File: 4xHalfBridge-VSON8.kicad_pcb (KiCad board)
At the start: 4 copper layers, 90 x 36 mm, 87 parts, among them U1 VSON8_Nexfet, U10 24LC01, U2 VSON8_Nexfet, U3 VSON8_Nexfet, U4 VSON8_Nexfet, U5 VSON8_Nexfet, U6 VSON8_Nexfet, U7 VSON8_Nexfet, U8 VSON8_Nexfet, U9 PowerStage_L

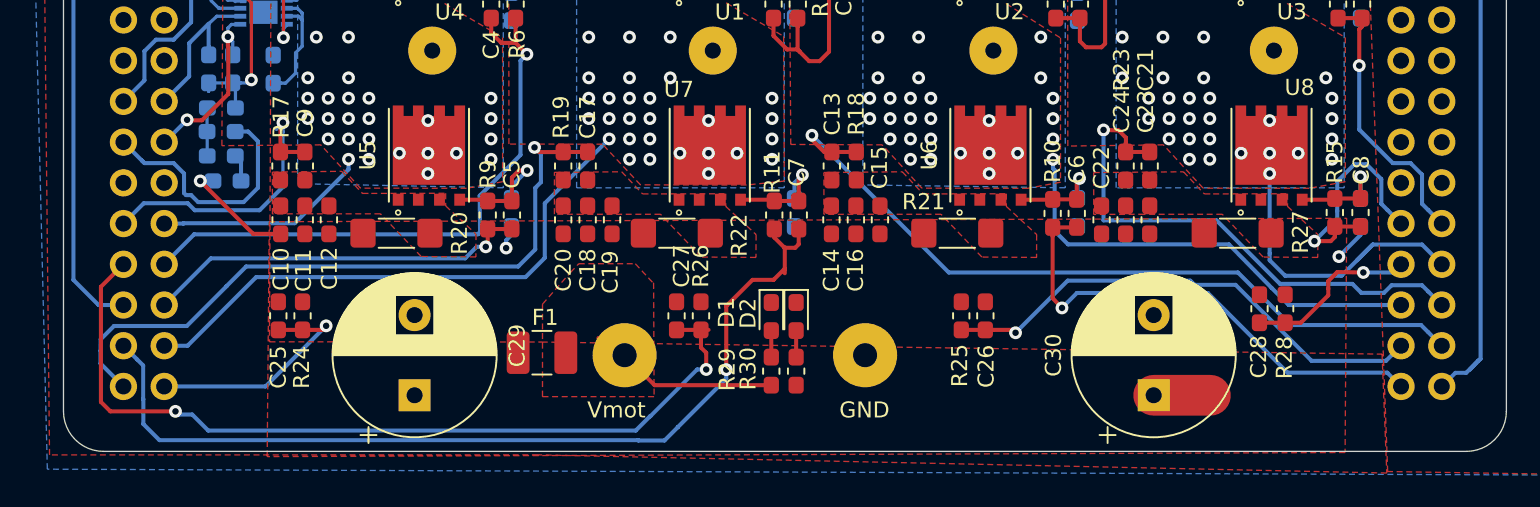
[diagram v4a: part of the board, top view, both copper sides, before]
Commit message: add voltage divider circuit for motor coil outpus
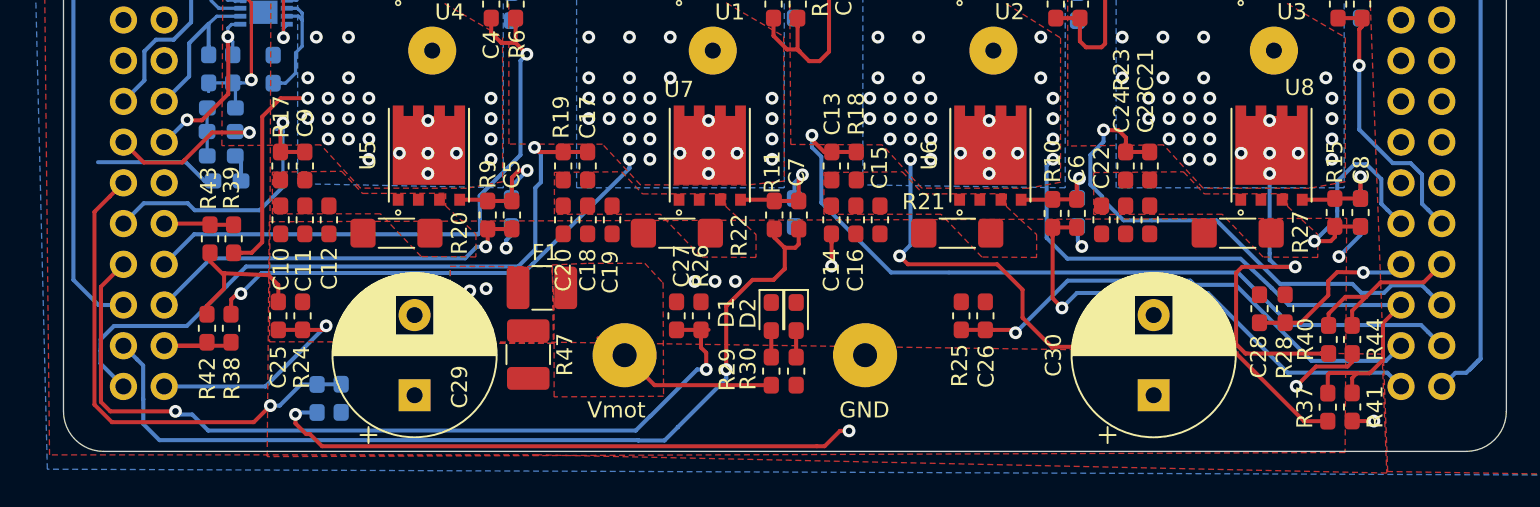
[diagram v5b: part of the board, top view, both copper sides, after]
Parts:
- added R37: R, Resistor_SMD:R_0603_1608Metric_Pad1.05x0.95mm_HandSolder, F.Cu at (78.9, 33.2)
- added R38: R, Resistor_SMD:R_0603_1608Metric_Pad1.05x0.95mm_HandSolder, F.Cu at (10.4, 28.3)
- added R39: R, Resistor_SMD:R_0603_1608Metric_Pad1.05x0.95mm_HandSolder, F.Cu at (10.6, 22.7)
- added R40: R, Resistor_SMD:R_0603_1608Metric_Pad1.05x0.95mm_HandSolder, F.Cu at (78.9, 29.0)
- added R41: R, Resistor_SMD:R_0603_1608Metric_Pad1.05x0.95mm_HandSolder, F.Cu at (80.4, 33.2)
- added R42: R, Resistor_SMD:R_0603_1608Metric_Pad1.05x0.95mm_HandSolder, F.Cu at (8.95, 28.3)
- added R43: R, Resistor_SMD:R_0603_1608Metric_Pad1.05x0.95mm_HandSolder, F.Cu at (9.14, 22.7)
- added R44: R, Resistor_SMD:R_0603_1608Metric_Pad1.05x0.95mm_HandSolder, F.Cu at (80.4, 29.0)
- added R45: R, Resistor_SMD:R_0603_1608Metric_Pad1.05x0.95mm_HandSolder, B.Cu at (15.8, 32.7)
- added R46: R, Resistor_SMD:R_0603_1608Metric_Pad1.05x0.95mm_HandSolder, B.Cu at (17.3, 32.7)
- added R47: R, Resistor_SMD:R_1210_3225Metric_Pad1.42x2.65mm_HandSolder, F.Cu at (29.0, 30.0)
- moved F1 4.05 mm to (29.8, 25.8)
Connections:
- C29 pad 1: /VDRAIN -> /MISENN
- C30 pad 1: /VDRAIN -> /MISENN
- C31 pad 1: /VDRAIN -> /MISENN
- C32 pad 1: /VDRAIN -> /MISENN
- C33 pad 1: /VDRAIN -> /MISENN
- C34 pad 1: /VDRAIN -> /MISENN
- F1 pad 1: /VDRAIN -> /MISENP
- R30 pad 2: /VDRAIN -> /MISENN
- U1 pad 3: /VDRAIN -> /MISENN
- U2 pad 3: /VDRAIN -> /MISENN
- U3 pad 3: /VDRAIN -> /MISENN
- U4 pad 3: /VDRAIN -> /MISENN
- U9 pad 13: Net-(U9-Pad13) -> /VSEN_VMOT
- U9 pad 16: /A -> /VSENA
- U9 pad 22: /B -> /VSENB
- U9 pad 42: /D -> /VSEND
- U9 pad 43: /C -> /VSENC
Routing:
- net /VSENC: track 0.00 -> 39.1 mm, vias 0 -> 1
- net /MISENN: track 0.00 -> 37.5 mm, vias 0 -> 22
- net /VSEN_VMOT: track 0.00 -> 31.4 mm, vias 0 -> 1
- net GND: track 21.0 -> 40.6 mm, vias 5 -> 11
- net /VSEND: track 0.00 -> 11.2 mm
- net /C: track 28.0 -> 38.3 mm
- net /VSENB: track 0.00 -> 7.02 mm
- net /5V: track 15.7 -> 10.2 mm, vias 0 -> 1
- net /B: track 40.3 -> 34.9 mm
- net /VSENA: track 0.00 -> 4.36 mm
- net /VDRAIN: track 3.54 -> 0.00 mm, vias 20 -> 0
- net /D: track 19.2 -> 21.5 mm, vias 29 -> 30
- net /CISENP: track 48.1 -> 50.2 mm
- net /A: track 13.5 -> 13.2 mm, vias 26 -> 25
- net /MISENP: vias 0 -> 5
- added copper zone on F.Cu, net /MISENN
- added copper zone on B.Cu, net /MISENP
- added copper zone on F.Cu, net /MISENP
- removed copper zone on F.Cu, net /VDRAIN
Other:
- copper layers 4 -> 2

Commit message: add files
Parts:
- removed C20, C21, C22, C23, C24, C25, C26, C27, C28: C, Capacitor_SMD:C_0603_1608Metric_Pad1.05x0.95mm_HandSolder
- removed C29, C30: CP, Capacitor_THT:CP_Radial_D10.0mm_P5.00mm
- removed C31, C32, C33, C34: CP, Capacitor_THT:CP_Radial_D5.0mm_P2.50mm
- removed C35: X7R, 47-nF, Capacitor_SMD:C_0603_1608Metric_Pad1.05x0.95mm_HandSolder
- removed the D2 at (45.7, 27.6)
- removed R40, R41, R42, R43, R44, R45, R46: R, Resistor_SMD:R_0603_1608Metric_Pad1.05x0.95mm_HandSolder
- removed R47: R, Resistor_SMD:R_1210_3225Metric_Pad1.42x2.65mm_HandSolder
- removed the U10 at (12.5, 8.61)
- added D2: D_Schottky, Diode_SMD:D_0603_1608Metric_Pad1.05x0.95mm_HandSolder, F.Cu at (14.0, 21.0)
- added D2: D_Schottky, Diode_SMD:D_0603_1608Metric_Pad1.05x0.95mm_HandSolder, F.Cu at (11.4, 20.1)
- added U9: VSON8_Nexfet, Custom_Mosfet:MOSFET_CSD19531Q5A, F.Cu at (75.2, 17.3)
- C1, C10, C11, C12, C13, C14, C15, C16, C17, C6, C7, C8, C9: footprint Capacitor_SMD:C_0603_1608Metric_Pad1.05x0.95mm_HandSolder -> Capacitor_SMD:C_0402_1005Metric
- C18, C19: value C -> CP; footprint Capacitor_SMD:C_0603_1608Metric_Pad1.05x0.95mm_HandSolder -> Capacitor_THT:CP_Radial_D10.0mm_P5.00mm
- C2, C3, C4, C5: footprint Capacitor_SMD:C_0603_1608Metric_Pad1.05x0.95mm_HandSolder -> Capacitor_THT:CP_Radial_D5.0mm_P2.00mm
- D3: moved to F.Cu
- D4: value D_Schottky -> LED; footprint Diode_SMD:D_0603_1608Metric_Pad1.05x0.95mm_HandSolder -> LED_SMD:LED_0603_1608Metric_Pad1.05x0.95mm_HandSolder; moved to F.Cu
- F1: footprint Fuse:Fuse_1210_3225Metric_Pad1.42x2.65mm_HandSolder -> Fuse:Fuse_0603_1608Metric_Pad1.05x0.95mm_HandSolder
- F2: footprint Fuse:Fuse_0603_1608Metric_Pad1.05x0.95mm_HandSolder -> Fuse:Fuse_1210_3225Metric_Pad1.42x2.65mm_HandSolder; moved to F.Cu
- R1, R18, R19, R2, R37, R38, R39, R5: value R -> R_Small; footprint Resistor_SMD:R_0603_1608Metric_Pad1.05x0.95mm_HandSolder -> Resistor_SMD:R_0402_1005Metric
- R10, R11, R15, R17, R23, R24, R25, R26, R28, R29, R6, R9: value R -> R_Small; footprint Resistor_SMD:R_0603_1608Metric_Pad1.05x0.95mm_HandSolder -> Resistor_SMD:R_0603_1608Metric
- R12, R13, R14, R16, R7, R8: value R -> R_Small; footprint Resistor_SMD:R_0603_1608Metric_Pad1.05x0.95mm_HandSolder -> Resistor_SMD:R_0603_1608Metric; moved to F.Cu
- R20, R21: value R -> R_Small; footprint Resistor_SMD:R_1806_4516Metric_Pad1.57x1.80mm_HandSolder -> Resistor_SMD:R_0402_1005Metric
- R22, R27: value R -> R_Small; footprint Resistor_SMD:R_1806_4516Metric_Pad1.57x1.80mm_HandSolder -> Resistor_SMD:R_0603_1608Metric
- R3, R35, R36, R4: value R -> R_Small; footprint Resistor_SMD:R_0603_1608Metric_Pad1.05x0.95mm_HandSolder -> Resistor_SMD:R_0402_1005Metric; moved to F.Cu
- R30: value R -> R_Small; footprint Resistor_SMD:R_0603_1608Metric_Pad1.05x0.95mm_HandSolder -> Resistor_SMD:R_1210_3225Metric
- R31, R32, R33, R34: value R -> R_Small; footprint Resistor_SMD:R_0603_1608Metric_Pad1.05x0.95mm_HandSolder -> Resistor_SMD:R_1210_3225Metric; moved to F.Cu
- U1: value VSON8_Nexfet -> 24LC01; footprint Custom_Mosfet:MOSFET_CSD19531Q5A -> Package_DFN_QFN:DFN-8-1EP_3x2mm_P0.5mm_EP1.75x1.45mm
- moved R37 69.6 mm to (9.41, 28.6)
- moved R5 65.9 mm to (14.0, 15.5), turned to 180 degrees
- moved R33 65.1 mm to (74.5, 24.0)
- moved C9 64.7 mm to (79.4, 12.3), turned to 180 degrees
- moved R4 55.5 mm to (8.61, 18.2)
- moved U5 54.1 mm to (75.2, 4.32)
- moved R9 54.0 mm to (79.9, 13.7), turned to 180 degrees
- moved R15 52.0 mm to (28.6, 9.53), turned to 180 degrees
- moved R17 50.1 mm to (62.9, 9.53), turned to 0 degrees
- moved R2 49.0 mm to (14.0, 18.4), turned to 180 degrees
- moved R24 48.8 mm to (62.9, 18.5), turned to 0 degrees
- moved C17 47.0 mm to (79.6, 16.9), turned to 180 degrees
- moved C3 46.7 mm to (34.5, 3.43)
- moved C2 46.6 mm to (17.0, 3.43)
- moved R32 45.8 mm to (54.5, 24.0)
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- renumbered U9 to U10
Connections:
- C1 pad 1: Net-(C1-Pad1) -> /CarrierBoard/5V
- C1 pad 2: /BHG -> GND
- C10 pad 2: Net-(C10-Pad2) -> /4xHalfBridge/VSENA
- C11 pad 2: Net-(C10-Pad2) -> /4xHalfBridge/VSENB
- C12 pad 2: Net-(C10-Pad2) -> /4xHalfBridge/VSENC
- C13 pad 1: Net-(C13-Pad1) -> GND
- C13 pad 2: /CISENP -> /4xHalfBridge/VSEND
- C14 pad 1: GND -> /4xHalfBridge/ALG
- C14 pad 2: Net-(C13-Pad1) -> Net-(C14-Pad2)
- C15 pad 1: GND -> /4xHalfBridge/BLG
- C15 pad 2: Net-(C13-Pad1) -> Net-(C15-Pad2)
- C16 pad 1: GND -> /4xHalfBridge/CLG
- C16 pad 2: Net-(C13-Pad1) -> Net-(C16-Pad2)
- C17 pad 1: Net-(C17-Pad1) -> /4xHalfBridge/DLG
- C17 pad 2: /BISENP -> Net-(C17-Pad2)
- C18 pad 1: GND -> /4xHalfBridge/VMOT
- C18 pad 2: Net-(C17-Pad1) -> GND
- C19 pad 1: GND -> /4xHalfBridge/VMOT
- C19 pad 2: Net-(C17-Pad1) -> GND
- C2 pad 1: Net-(C2-Pad1) -> /4xHalfBridge/VMOT
- C2 pad 2: /CHG -> GND
- C3 pad 1: Net-(C3-Pad1) -> /4xHalfBridge/VMOT
- C3 pad 2: /DHG -> GND
- C4 pad 1: Net-(C4-Pad1) -> /4xHalfBridge/VMOT
- C4 pad 2: /AHG -> GND
- C5 pad 1: Net-(C5-Pad1) -> /4xHalfBridge/VMOT
- C5 pad 2: /ALG -> GND
- C6 pad 1: Net-(C6-Pad1) -> /4xHalfBridge/AHG
- C6 pad 2: /CLG -> Net-(C6-Pad2)
- C7 pad 1: Net-(C7-Pad1) -> /4xHalfBridge/BHG
- C7 pad 2: /BLG -> Net-(C7-Pad2)
- C8 pad 1: Net-(C8-Pad1) -> /4xHalfBridge/CHG
- C8 pad 2: /DLG -> Net-(C8-Pad2)
- C9 pad 1: Net-(C10-Pad2) -> /4xHalfBridge/DHG
- C9 pad 2: /AISENP -> Net-(C9-Pad2)
- D4 pad 1: Net-(C35-Pad1) -> GND
- F1 pad 1: /MISENP -> /CarrierBoard/5V_IN_RAW
- F1 pad 2: VCC -> Net-(D2-Pad2)
- F2 pad 1: /5V -> /4xHalfBridge/VMOT
- F2 pad 2: Net-(D4-Pad2) -> VCC
- R1 pad 1: Net-(C1-Pad1) -> Net-(R1-Pad1)
- R1 pad 2: /BHG -> /CarrierBoard/5V
- R10 pad 1: Net-(C6-Pad1) -> Net-(C6-Pad2)
- R10 pad 2: /CLG -> GND
- R11 pad 1: Net-(C7-Pad1) -> Net-(C7-Pad2)
- R11 pad 2: /BLG -> GND
- R12 pad 1: Net-(C5-Pad1) -> GND
- R12 pad 2: GND -> Net-(C8-Pad2)
- R13 pad 1: Net-(C6-Pad1) -> Net-(C9-Pad2)
- R14 pad 1: Net-(C7-Pad1) -> Net-(R14-Pad1)
- R14 pad 2: GND -> /4xHalfBridge/VSENA
- R15 pad 1: Net-(C8-Pad1) -> Net-(R15-Pad1)
- R15 pad 2: /DLG -> /4xHalfBridge/VSENB
- R16 pad 1: Net-(C8-Pad1) -> Net-(R16-Pad1)
- R16 pad 2: GND -> /4xHalfBridge/VSENC
- R17 pad 1: Net-(C10-Pad2) -> /4xHalfBridge/VSEND
- R17 pad 2: /AISENP -> Net-(R17-Pad2)
- R18 pad 1: Net-(C13-Pad1) -> GND
- R18 pad 2: /CISENP -> /4xHalfBridge/VSENA
- R19 pad 1: Net-(C17-Pad1) -> GND
- R19 pad 2: /BISENP -> /4xHalfBridge/VSENB
- R2 pad 1: Net-(C2-Pad1) -> /CarrierBoard/5V
- R2 pad 2: /CHG -> /CarrierBoard/EEPROM_SDA
- R20 pad 1: Net-(C10-Pad2) -> GND
- R20 pad 2: GND -> /4xHalfBridge/VSENC
- R21 pad 1: Net-(C13-Pad1) -> GND
- R21 pad 2: GND -> /4xHalfBridge/VSEND
- R22 pad 1: Net-(C17-Pad1) -> /4xHalfBridge/ALG
- R22 pad 2: GND -> Net-(C14-Pad2)
- R23 pad 1: Net-(C21-Pad1) -> /4xHalfBridge/BLG
- R23 pad 2: /DISENP -> Net-(C15-Pad2)
- R24 pad 1: GND -> Net-(C16-Pad2)
- R24 pad 2: /AISENN -> /4xHalfBridge/CLG
- R25 pad 1: GND -> /4xHalfBridge/DLG
- R25 pad 2: /CISENN -> Net-(C17-Pad2)
- R26 pad 1: GND -> Net-(C14-Pad2)
- R26 pad 2: /BISENN -> GND
- R27 pad 1: Net-(C21-Pad1) -> Net-(C15-Pad2)
- R28 pad 1: GND -> Net-(C16-Pad2)
- R28 pad 2: /DISENN -> GND
- R29 pad 1: Net-(D1-Pad2) -> Net-(C17-Pad2)
- R29 pad 2: VCC -> GND
- R3 pad 1: Net-(C1-Pad1) -> /CarrierBoard/5V
- R3 pad 2: GND -> /CarrierBoard/EEPROM_SCL
- R30 pad 1: Net-(D2-Pad2) -> /4xHalfBridge/AISENN
- R30 pad 2: /MISENN -> /4xHalfBridge/AISENP
- R31 pad 1: Net-(D3-Pad2) -> /4xHalfBridge/AISENN
- R31 pad 2: Net-(D4-Pad2) -> /4xHalfBridge/BISENP
- R32 pad 1: Net-(C35-Pad1) -> /4xHalfBridge/AISENN
- R32 pad 2: Net-(R32-Pad2) -> /4xHalfBridge/CISENP
- R33 pad 1: Net-(C35-Pad1) -> /4xHalfBridge/AISENN
- R33 pad 2: /SDA -> /4xHalfBridge/DISENP
- R34 pad 1: Net-(C35-Pad1) -> GND
- R34 pad 2: /SCL -> /4xHalfBridge/AISENN
- R35 pad 1: /WP -> Net-(D2-Pad2)
- R35 pad 2: Net-(R35-Pad2) -> Net-(D1-Pad2)
- R36 pad 1: Net-(R36-Pad1) -> /4xHalfBridge/VMOT
- R36 pad 2: GND -> /CarrierBoard/VSEN_VMOT
- R37 pad 1: /C -> VCC
- R37 pad 2: /VSENC -> Net-(D3-Pad2)
- R38 pad 1: /B -> /4xHalfBridge/VMOT
- R38 pad 2: /VSENB -> Net-(D4-Pad2)
- R39 pad 1: /A -> /CarrierBoard/VSEN_VMOT
- R39 pad 2: /VSENA -> GND
- R4 pad 1: Net-(C2-Pad1) -> Net-(R4-Pad1)
- R5 pad 1: Net-(C3-Pad1) -> /CarrierBoard/EEPROM_WP
- R5 pad 2: /DHG -> Net-(R1-Pad1)
- R6 pad 1: Net-(C4-Pad1) -> /4xHalfBridge/AHG
- R6 pad 2: /AHG -> Net-(C6-Pad2)
- R7 pad 1: Net-(C3-Pad1) -> /4xHalfBridge/BHG
- R7 pad 2: GND -> Net-(C7-Pad2)
- R8 pad 1: Net-(C4-Pad1) -> Net-(C8-Pad2)
- R8 pad 2: GND -> /4xHalfBridge/CHG
- R9 pad 1: Net-(C5-Pad1) -> /4xHalfBridge/DHG
- R9 pad 2: /ALG -> Net-(C9-Pad2)
- U1 pad 1: /B -> Net-(R4-Pad1)
- U1 pad 2: Net-(C1-Pad1) -> Net-(R4-Pad1)
- U1 pad 3: /MISENN -> Net-(R4-Pad1)
- U10 pad 10: /SCL -> /4xHalfBridge/VSENB
- U10 pad 11: /5V -> /4xHalfBridge/AHG
- U10 pad 12: /SDA -> /4xHalfBridge/ALG
- U10 pad 13: /VSEN_VMOT -> /4xHalfBridge/AISENP
- U10 pad 14: Net-(U9-Pad14) -> /4xHalfBridge/VSENC
- U10 pad 15: /AISENP -> /4xHalfBridge/BISENP
- U10 pad 16: /VSENA -> /4xHalfBridge/BLG
- U10 pad 17: /BISENN -> /4xHalfBridge/BHG
- U10 pad 18: /AHG -> /4xHalfBridge/VSEND
- U10 pad 19: /BHG -> /4xHalfBridge/CHG
- U10 pad 2: Net-(U9-Pad2) -> /CarrierBoard/5V_IN_RAW
- U10 pad 20: /ALG -> /4xHalfBridge/CLG
- U10 pad 21: /BLG -> /4xHalfBridge/CISENP
- U10 pad 22: /VSENB -> /4xHalfBridge/DISENP
- U10 pad 23: /BISENP -> /4xHalfBridge/DHG
- U10 pad 24: /AISENN -> /4xHalfBridge/DLG
- U10 pad 3: Net-(U9-Pad3) -> /CarrierBoard/VSEN_VMOT
- U10 pad 39: /DLG -> Net-(U10-Pad39)
- U10 pad 40: /DHG -> Net-(U10-Pad40)
- U10 pad 41: /DISENN -> Net-(U10-Pad41)
- U10 pad 42: /VSEND -> Net-(U10-Pad42)
- U10 pad 43: /VSENC -> Net-(U10-Pad43)
- U10 pad 44: /DISENP -> Net-(U10-Pad44)
- U10 pad 45: /CISENN -> Net-(U10-Pad45)
- U10 pad 46: /CISENP -> Net-(U10-Pad46)
- U10 pad 47: /CLG -> Net-(U10-Pad47)
- U10 pad 48: /CHG -> Net-(U10-Pad48)
- U10 pad 5: Net-(U9-Pad5) -> /CarrierBoard/EEPROM_WP
- U10 pad 6: Net-(U9-Pad6) -> /CarrierBoard/EEPROM_SCL
- U10 pad 7: Net-(U9-Pad7) -> /CarrierBoard/EEPROM_SDA
- U10 pad 9: /WP -> /4xHalfBridge/VSENA
- U2 pad 1: /C -> Net-(R14-Pad1)
- U2 pad 2: Net-(C2-Pad1) -> Net-(C6-Pad2)
- U2 pad 3: /MISENN -> /4xHalfBridge/VMOT
- U3 pad 1: /D -> Net-(R15-Pad1)
- U3 pad 2: Net-(C3-Pad1) -> Net-(C7-Pad2)
- U3 pad 3: /MISENN -> /4xHalfBridge/VMOT
- U4 pad 1: /A -> Net-(R16-Pad1)
- U4 pad 2: Net-(C4-Pad1) -> Net-(C8-Pad2)
- U4 pad 3: /MISENN -> /4xHalfBridge/VMOT
- U5 pad 1: Net-(C10-Pad2) -> Net-(R17-Pad2)
- U5 pad 2: Net-(C5-Pad1) -> Net-(C9-Pad2)
- U5 pad 3: /A -> /4xHalfBridge/VMOT
- U6 pad 1: Net-(C13-Pad1) -> /4xHalfBridge/AISENP
- U6 pad 2: Net-(C6-Pad1) -> Net-(C14-Pad2)
- U6 pad 3: /C -> Net-(R14-Pad1)
- U7 pad 1: Net-(C17-Pad1) -> /4xHalfBridge/BISENP
- U7 pad 2: Net-(C7-Pad1) -> Net-(C15-Pad2)
- U7 pad 3: /B -> Net-(R15-Pad1)
- U8 pad 1: Net-(C21-Pad1) -> /4xHalfBridge/CISENP
- U8 pad 2: Net-(C8-Pad1) -> Net-(C16-Pad2)
- U8 pad 3: /D -> Net-(R16-Pad1)
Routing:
- net GND: track 40.6 -> 151.4 mm, vias 11 -> 9
- net /4xHalfBridge/DHG: track 0.00 -> 100.7 mm, vias 0 -> 3
- net /BHG: track 91.8 -> 0.00 mm, vias 1 -> 0
- net /4xHalfBridge/DLG: track 0.00 -> 90.6 mm, vias 0 -> 3
- net /4xHalfBridge/DISENP: track 0.00 -> 70.7 mm, vias 0 -> 1
- net /4xHalfBridge/CHG: track 0.00 -> 70.3 mm, vias 0 -> 1
- net /4xHalfBridge/VSEND: track 0.00 -> 70.0 mm, vias 0 -> 1
- net /CHG: track 68.5 -> 0.00 mm, vias 1 -> 0
- net /4xHalfBridge/CLG: track 0.00 -> 66.4 mm, vias 0 -> 1
- net /BLG: track 57.7 -> 0.00 mm, vias 1 -> 0
- net /4xHalfBridge/BHG: track 0.00 -> 57.4 mm, vias 0 -> 1
- net /BISENN: track 53.8 -> 0.00 mm, vias 2 -> 0
- net /4xHalfBridge/CISENP: track 0.00 -> 53.2 mm, vias 0 -> 1
- net /4xHalfBridge/VSENC: track 0.00 -> 52.8 mm, vias 0 -> 1
- net /CISENP: track 50.2 -> 0.00 mm, vias 1 -> 0
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- added copper zone on B.Cu, net /4xHalfBridge/AISENN
- added copper zone on F.Cu, net /4xHalfBridge/AISENN
- added copper zone on F.Cu, net /4xHalfBridge/AISENP
- added copper zone on F.Cu, net /4xHalfBridge/BISENP
- added copper zone on F.Cu, net /4xHalfBridge/CISENP
- added copper zone on F.Cu, net /4xHalfBridge/DISENP
- added copper zone on F.Cu, net /4xHalfBridge/VMOT
- added copper zone on F.Cu, net Net-(R14-Pad1)
- added copper zone on F.Cu, net Net-(R15-Pad1)
- added copper zone on F.Cu, net Net-(R16-Pad1)
- added copper zone on F.Cu, net Net-(R17-Pad2)
- removed copper zone on B.Cu, net /A
- removed copper zone on F.Cu, net /A
- removed copper zone on B.Cu, net /B
- removed copper zone on F.Cu, net /B
- removed copper zone on B.Cu, net /C
- removed copper zone on F.Cu, net /C
- removed copper zone on B.Cu, net /D
- removed copper zone on F.Cu, net /D
- removed copper zone on F.Cu, net /MISENN
- removed copper zone on B.Cu, net /MISENP
- removed copper zone on F.Cu, net /MISENP
- removed copper zone on F.Cu, net Net-(C10-Pad2)
- removed copper zone on F.Cu, net Net-(C13-Pad1)
- removed copper zone on F.Cu, net Net-(C17-Pad1)
- removed copper zone on F.Cu, net Net-(C21-Pad1)
- removed copper zone on B.Cu, net Net-(C35-Pad1)
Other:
- board text removed: "GND"
- board text removed: "Vmot"
